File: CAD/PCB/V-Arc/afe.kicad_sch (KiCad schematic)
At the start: 10 parts, among them J3 AudioJack2, SW1 SW_SPDT, U5 TL072

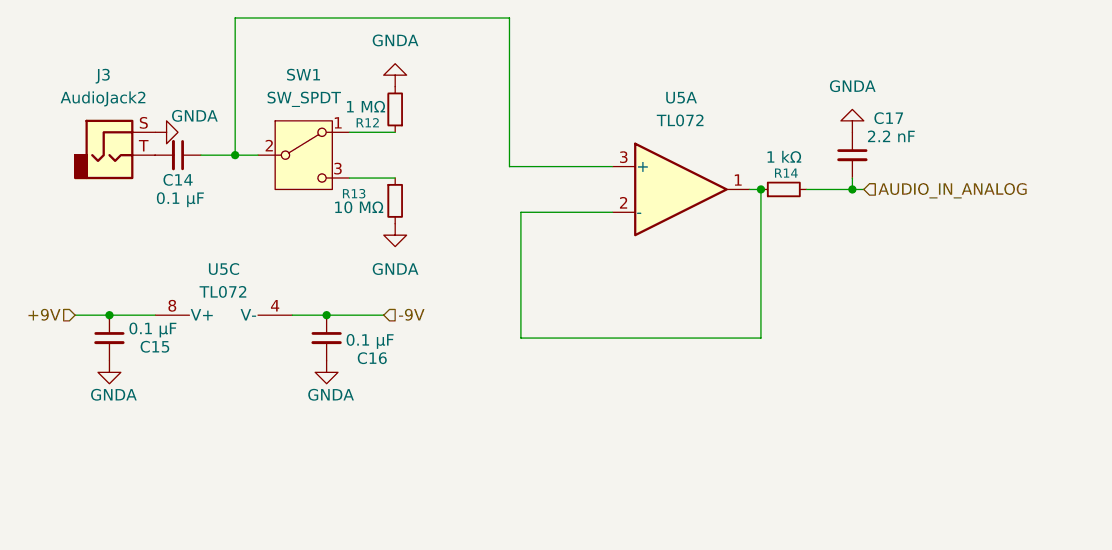
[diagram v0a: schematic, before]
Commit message: Added a sheet and organized
-Added XIAO ESP32 Core sheet
-Titled all sheets
-Added power switch to the power sheet
-Organized all sheets with text boxes
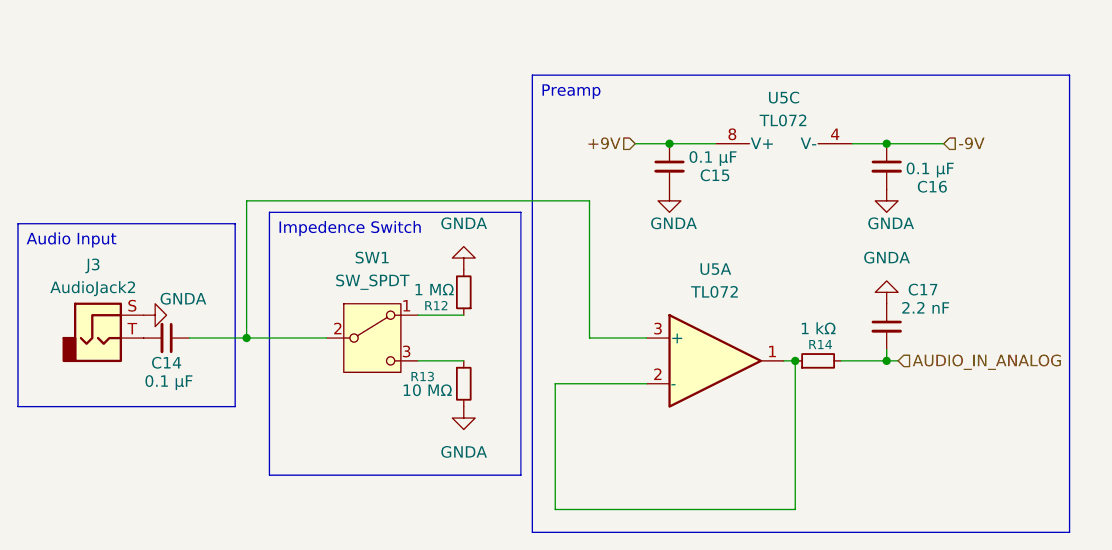
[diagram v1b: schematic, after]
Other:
- title: (none) -> V-Arc Analog Front End
- moved on the sheet: C14, C15, C16, C17, J3, R12, R13, R14, SW1, U5A, U5C
